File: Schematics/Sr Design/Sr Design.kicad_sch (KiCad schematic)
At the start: 0 parts

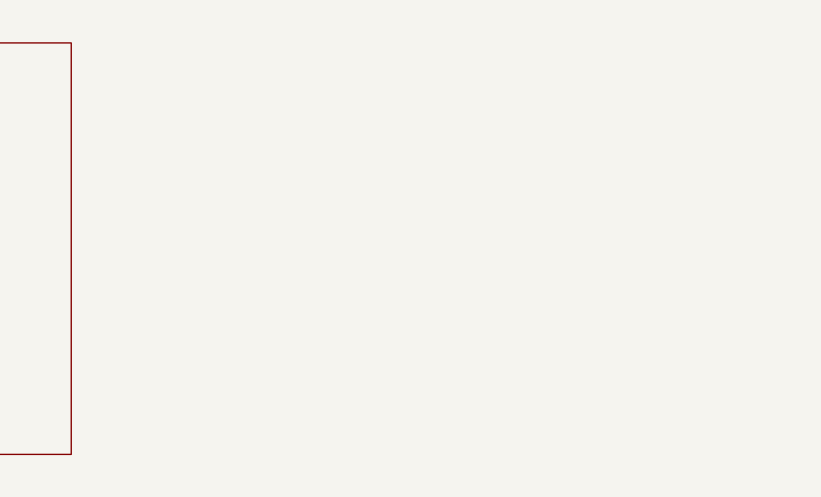
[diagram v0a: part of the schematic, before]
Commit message: SCHM updated need to figure out how we want to apply our power design.
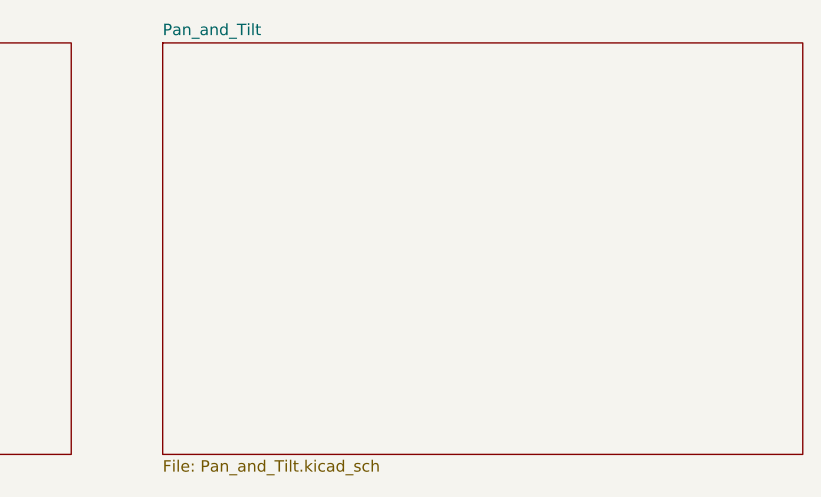
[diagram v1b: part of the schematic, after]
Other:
- added sheet Pan_and_Tilt (Pan_and_Tilt.kicad_sch)
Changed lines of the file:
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@@
+		)
+	)
+	(sheet
+		(at 106.68 19.05)
+		(size 71.12 45.72)
+		(exclude_from_sim no)
+		(in_bom yes)
+		(on_board yes)
+		(dnp no)
+		(fields_autoplaced yes)
+		(stroke
+			(width 0.1524)
+			(type solid)
+		)
+		(fill
+			(color 0 0 0 0.0000)
+		)
+		(property "Sheetname" "Pan_and_Tilt"
+			(at 106.68 18.3384 0)
+			(effects
+				(font
+					(size 1.27 1.27)
+				)
+				(justify left bottom)
+			)
+		)
+		(property "Sheetfile" "Pan_and_Tilt.kicad_sch"
+			(at 106.68 65.3546 0)
+			(effects
+				(font
+					(size 1.27 1.27)
+				)
+				(justify left top)
+			)
+		)
+		(instances
+			(project "Sr Design"
+				(path "/a9415093-c716-43d5-965a-b0cfe44093a0"
+					(page "3")
+				)
+			)
 		)
 	)

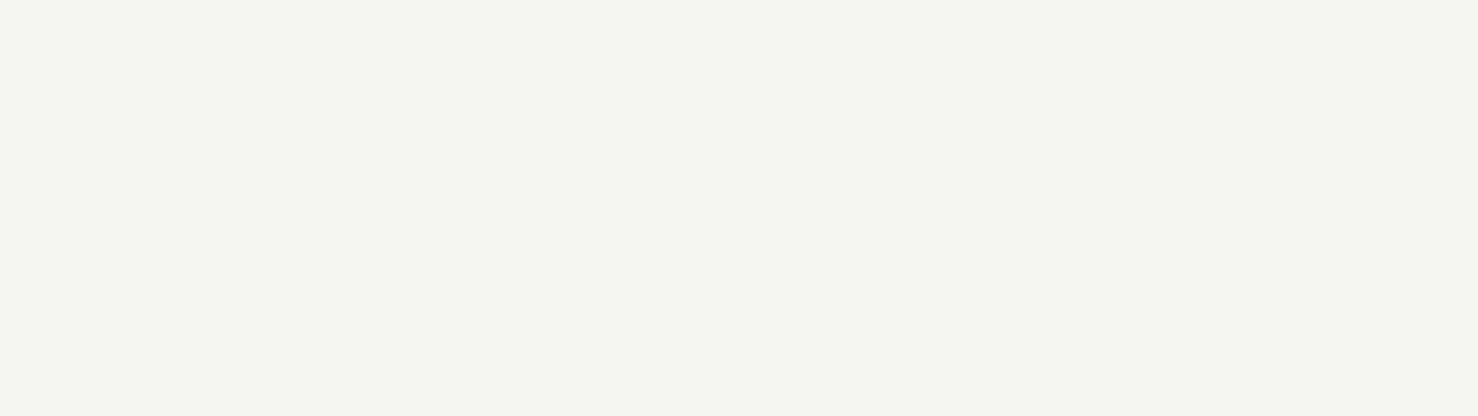
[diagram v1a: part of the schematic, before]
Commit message: schematics updated
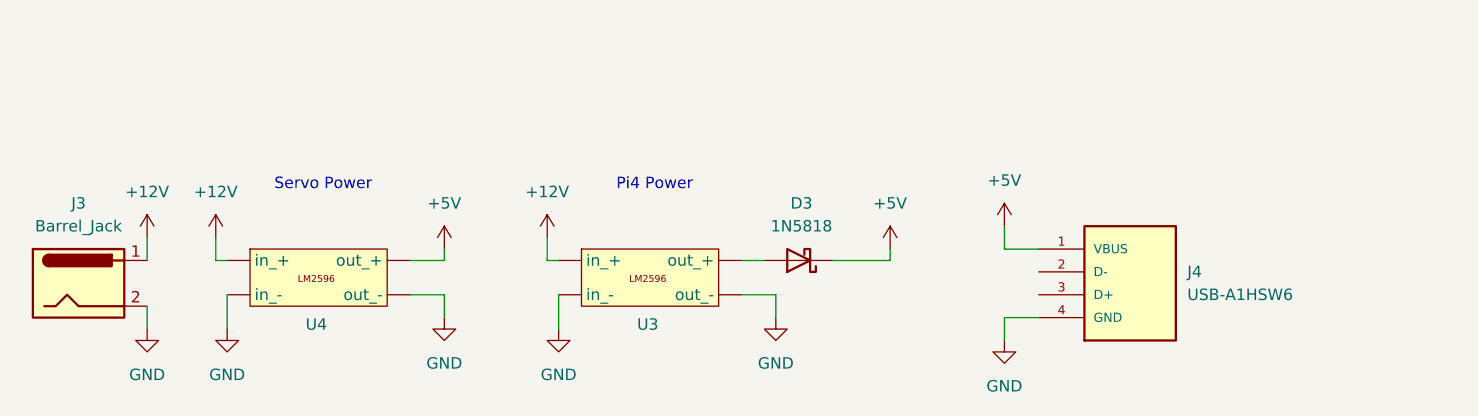
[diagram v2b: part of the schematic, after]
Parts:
- added D3: 1N5818, Diode_THT:D_DO-41_SOD81_P10.16mm_Horizontal, symbol Diode:1N5818
- added J3: Barrel_Jack, symbol Connector:Barrel_Jack
- added J4: USB-A1HSW6, USB-A1HSW6:OST_USB-A1HSW6, symbol USB-A1HSW6:USB-A1HSW6
- added U3, U4: ~, symbol Turret_Power:_LM2596_Buck_Converter
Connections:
- new net: D3.2 (A), U3. (out_-)
- new net +12V: J3.1, U3. (out_-), U4. (out_-)
- new net +5V: D3.1 (K), J4.1 (VBUS), U4. (out_-)
- new net GND: J3.2, J4.4 (GND), U3. (out_-), U4. (out_-)
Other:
- note added: "Pi4 Power"
- note added: "Servo Power"
